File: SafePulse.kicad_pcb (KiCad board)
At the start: 4 copper layers, 40.6 x 20.8 mm, 87 parts, among them IC1 S-35770E01I-K8T2U, J1 Conn_01x03_Male, J2 4208, Q1 FQT7N10L, Q2 BC846A, Q3 MMBT3906, Q4 MMBT3906, U1 TS4061AICT-1.25, U2 74HC14, U33 MAX9910EXK+T, U4 CD14538BM

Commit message: Added changes of Allan
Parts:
- moved REF** 0.08 mm to (156.4, 63.6)
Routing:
- net Net-(D8-A): track 4.88 -> 3.87 mm
- net Net-(D1-A): track 2.20 -> 1.52 mm
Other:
- outline, holes or cut-outs redrawn

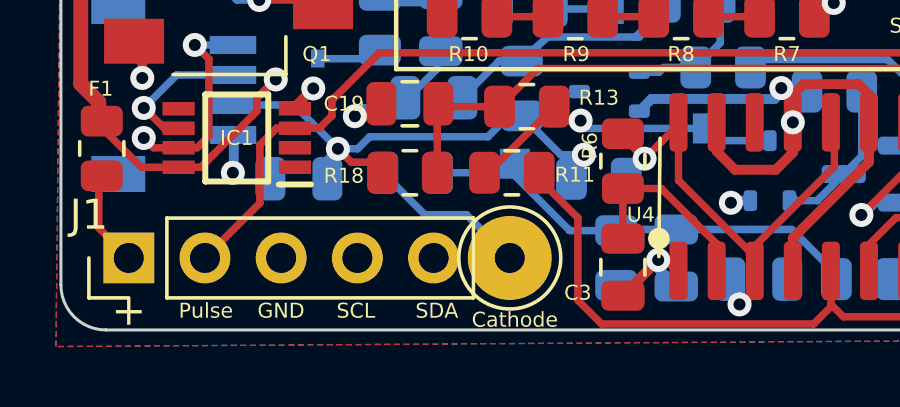
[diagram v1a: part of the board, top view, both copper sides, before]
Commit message: Aligned labels on board and replaces text labels in schematics
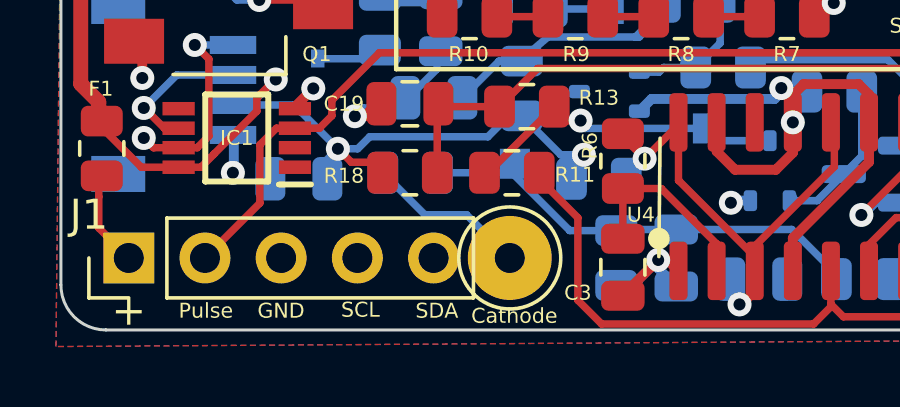
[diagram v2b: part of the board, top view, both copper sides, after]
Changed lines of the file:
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@@
 		)
 		(fp_text user "${VALUE}"
-			(at -1.19 -2.22 0)
+			(at -1.6764 -2.22 0)
 			(layer "B.SilkS")
 			(effects
@@
 		)
 		(fp_text user "${VALUE}"
-			(at -2.22 1.25 0)
+			(at -2.2352 1.5748 0)
 			(layer "B.SilkS")
 			(effects
@@
 		)
 		(property "Value" "Cathode"
-			(at 0.17 2.06 0)
+			(at 0.1524 1.9304 0)
 			(layer "F.SilkS")
 			(effects
@@
 	)
 	(gr_text "SCL\n"
-		(at 136.07 77.325 0)
+		(at 136.2216 77.2922 0)
 		(layer "F.SilkS")
 		(effects
@@
 	)
 	(gr_text "SCL"
-		(at 136.07 76.925 0)
+		(at 136.12 77.2414 0)
 		(layer "B.SilkS")
 		(effects
@@
 	)
 	(gr_text "SDA"
-		(at 138.77 76.925 0)
+		(at 138.8124 77.2922 0)
 		(layer "B.SilkS")
 		(effects

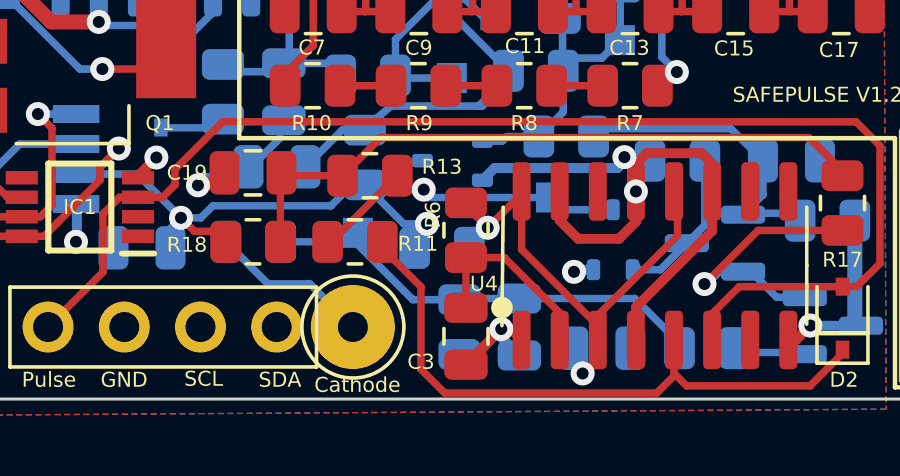
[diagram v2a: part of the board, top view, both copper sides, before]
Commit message: Moved anode 01 inch..
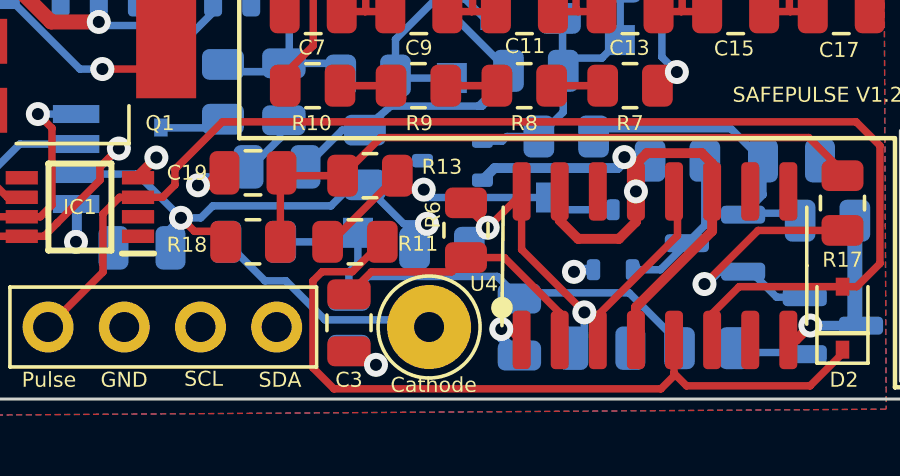
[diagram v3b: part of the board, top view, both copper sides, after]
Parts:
- moved C3 3.93 mm to (141.1, 75.4)
- moved R22 3.68 mm to (141.1, 75.4)
- moved H1 2.54 mm to (143.7, 75.6)
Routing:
- net Net-(D2-K): track 21.2 -> 25.8 mm
- net GND: track 54.6 -> 51.2 mm, vias 14 -> 15
- net Net-(U4A-RxCx): track 7.16 -> 9.90 mm
- net Net-(H1-Pad1): track 6.11 -> 8.03 mm
- net Net-(C22-Pad1): track 15.2 -> 16.8 mm
- net Net-(U4A-R): track 17.3 -> 18.0 mm

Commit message: V2.0.0
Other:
- board text added: "SAFEPULSE V2.0.0"
- board text removed: "SAFEPULSE V1.2.6"
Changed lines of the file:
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@@
 	(title_block
 		(title "SafePulse High Voltage Geiger Muller Power Supply")
-		(date "2025-04-03")
-		(rev "V1.2.6")
+		(date "2025-04-12")
+		(rev "V2.0.0")
 		(comment 1 "Double Sided Version With Counter")
 	)
@@
 			(psa4output no)
 			(plot_black_and_white yes)
-			(plotinvisibletext no)
 			(sketchpadsonfab no)
 			(plotpadnumbers no)
@@
 			(layer "F.Fab")
 		)
-		(fp_text user "${REFERENCE}"
-			(at 0 0 0)
-			(layer "F.Fab")
-			(hide yes)
-			(effects
-				(font
-					(size 1.27 1.27)
-					(thickness 0.254)
-				)
-			)
-		)
 		(pad "1" smd rect
 			(at -1.938 -0.975 270)
@@
 			(layer "B.Fab")
 		)
-		(fp_text user "${REFERENCE}"
-			(at 0 0 270)
-			(layer "B.Fab")
-			(hide yes)
-			(effects
-				(font
-					(size 1.27 1.27)
-					(thickness 0.254)
-				)
-				(justify mirror)
-			)
-		)
 		(pad "1" smd rect
 			(at -1.5 1.975 90)
@@
 		)
 	)
-	(gr_text "SAFEPULSE V1.2.6\n"
+	(gr_text "SAFEPULSE V2.0.0\n"
 		(at 157.02 67.825 0)
 		(layer "F.SilkS")
@@
 		)
 	)
-	(gr_text "SAFEPULSE V1.2.6\n"
+	(gr_text "SAFEPULSE V2.0.0\n"
 		(at 130.87 77.365 0)
 		(layer "B.SilkS")

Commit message: Cleaned up files . JLCPCB production files generated for V2.0.0
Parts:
- removed REF**: LOGO, Library:QR_code_SafePulse
- added C20: 100pF, Capacitor_SMD:C_0805_2012Metric, B.Cu at (142.8, 63.6)
- added C21: 0.1uF, Capacitor_SMD:C_0805_2012Metric, B.Cu at (135.5, 70.2)
- added G3: LOGO, Symbol:HV warning, F.Cu at (159.8, 67.0)
- added G3: LOGO, Symbol:HV warning, B.Cu at (163.5, 68.7)
- added R2: 10M, Resistor_SMD:R_1206_3216Metric, F.Cu at (165.4, 67.2)
- added R26: 22M, Resistor_SMD:R_0805_2012Metric, B.Cu at (145.1, 65.3)
- C1: value 150pF -> 110pF
- C22: value 1.5nF -> 390pF
- C3: value 10nF -> 1nF
- C4: value 10uF -> 47uF
- H2: value Anode -> LND712
- H4: value Anode -> LND7317
- J2: value 4208 -> JST SM04B-SRSS-TB(LF)(SN)
- R22: value 12K -> 20K
- R24: value 22k -> 33k
- TP7: moved to B.Cu
- moved R24 6.51 mm to (150.1, 60.0), turned to -90 degrees
- moved TP1 2.39 mm to (151.4, 68.0)
- moved U33 2.17 mm to (145.2, 62.2), turned to 180 degrees
- moved R23 1.85 mm to (147.8, 60.0), turned to 90 degrees
- moved TP7 1.32 mm to (165.5, 67.2), turned to 180 degrees
- moved R27 0.72 mm to (147.8, 63.7)
- moved TP2 0.48 mm to (144.4, 67.7)
- moved TP6 0.46 mm to (140.9, 58.7)
- moved C25 0.43 mm to (150.1, 63.7)
- moved R7 0.42 mm to (150.1, 67.7)
- moved R8 0.32 mm to (146.7, 67.7)
- moved R20 0.30 mm to (147.1, 67.2)
- moved R9 0.24 mm to (143.3, 67.7)
- moved R1 0.23 mm to (163.1, 67.2)
- moved R10 0.21 mm to (139.9, 67.7)
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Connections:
- C3 pad 2: GND -> Net-(U4A-VSS)
- H4 pad 1: Net-(H2-Pad1) -> Net-(H4-Pad1)
- IC1 pad 1: unconnected-(IC1-~RST-Pad1) -> +3V3
- R1 pad 2: Net-(H2-Pad1) -> Net-(H4-Pad1)
- U4 pad 1: GND -> Net-(U4A-VSS)
- U4 pad 11: GND -> Net-(U4A-R)
- U4 pad 12: Net-(U4A-R) -> GND
- U4 pad 13: GND -> Net-(U4A-R)
- U4 pad 14: unconnected-(U4B-RxCx-Pad14) -> GND
- U4 pad 15: GND -> unconnected-(U4B-VSS-Pad15)
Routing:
- net Net-(H4-Pad1): track 0.00 -> 8.12 mm
- net Net-(U4A-VSS): track 0.00 -> 7.41 mm
- net GND: track 51.2 -> 56.9 mm, vias 15 -> 7
- net Net-(U4A-R): track 18.0 -> 23.2 mm
- net +1V2: track 11.7 -> 15.5 mm
- net Net-(H2-Pad1): track 7.24 -> 3.61 mm
- net Net-(D9-A): track 11.8 -> 15.2 mm, vias 0 -> 1
- net Net-(IC1-SDA): track 20.3 -> 17.0 mm
- net Net-(U33-+): track 5.26 -> 2.46 mm
- net Net-(U33-V+): track 13.1 -> 15.8 mm
- net +3V3: track 39.1 -> 41.2 mm
- net Net-(C20-Pad2): track 7.32 -> 9.28 mm
- net Net-(C20-Pad1): track 0.00 -> 1.70 mm
- net Net-(C6-Pad2): track 13.0 -> 13.8 mm
- net Net-(U33--): track 15.4 -> 14.7 mm
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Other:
- board text added: "Anode"
- board text added: "HIGH VOLTAGE 500V !!"
- board text added: "SafePulse High Voltage Geiger-Muller Power Supply Ver 2.0.0 02 Nov 2025"
